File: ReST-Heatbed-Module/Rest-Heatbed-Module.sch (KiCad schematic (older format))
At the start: 16 parts, among them P1 02-SCREW-TERM, P2 02X04-MALE, P3 02-SCREW-TERM, P4 01X02-MALE, P5 02-SCREW-TERM, Q1 Q_BSH105, Q2 Q_AOT240L

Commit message: Moved Folders + Heatbed PCB Finished
If there is any problem, please post an issue or write a post on the stm32duino forum. I can assure there is going to be a problem again with the libraries used, would really appreciate it to get some suggestions onto how to manage that
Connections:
- net +3V3: now also P2.3 (P3); no longer P2.2 (P2)
- net +5V: now also P2.5 (P5), P2.6 (P6); no longer P2.1 (P1), P2.3 (P3)
- net GND: now also P1.2 (P2); no longer P1.1 (P1)
- net PWM-HEATBED: now also P2.1 (P1); no longer P2.6 (P6)
- net T0: now also P2.2 (P2); no longer P2.5 (P5)
- net at F1.1: now also P1.1 (P1); no longer P1.2 (P2)
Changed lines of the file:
@@
-$EndComp
-$Comp
-L CONN_02X04 P2
-U 1 1 56A6927C
-P 4750 2650
-F 0 "P2" H 4750 2900 50  0000 C CNN
-F 1 "02X04-MALE" H 4750 2400 50  0000 C CNN
-F 2 "Pin_Headers:Pin_Header_Angled_2x04" H 4750 1450 50  0001 C CNN
-F 3 "" H 4750 1450 50  0000 C CNN
-	1    4750 2650
-	1    0    0    -1
 $EndComp
 $Comp
@@
 F 3 "" H 2950 2550 50  0000 C CNN
 	1    2950 2550
-	-1   0    0    1
+	-1   0    0    -1
 $EndComp
 $Comp
@@
 L +5V #PWR05
 U 1 1 56A6A1BB
-P 4400 2400
-F 0 "#PWR05" H 4400 2250 50  0001 C CNN
-F 1 "+5V" H 4400 2540 50  0000 C CNN
-F 2 "" H 4400 2400 50  0000 C CNN
-F 3 "" H 4400 2400 50  0000 C CNN
-	1    4400 2400
+P 4300 2700
+F 0 "#PWR05" H 4300 2550 50  0001 C CNN
+F 1 "+5V" H 4300 2840 50  0000 C CNN
+F 2 "" H 4300 2700 50  0000 C CNN
+F 3 "" H 4300 2700 50  0000 C CNN
+	1    4300 2700
 	1    0    0    -1
 $EndComp
@@
 L +3V3 #PWR06
 U 1 1 56A6A1DD
-P 5100 2400
-F 0 "#PWR06" H 5100 2250 50  0001 C CNN
-F 1 "+3V3" H 5100 2540 50  0000 C CNN
-F 2 "" H 5100 2400 50  0000 C CNN
-F 3 "" H 5100 2400 50  0000 C CNN
-	1    5100 2400
-	1    0    0    -1
+P 5350 2600
+F 0 "#PWR06" H 5350 2450 50  0001 C CNN
+F 1 "+3V3" H 5350 2740 50  0000 C CNN
+F 2 "" H 5350 2600 50  0000 C CNN
+F 3 "" H 5350 2600 50  0000 C CNN
+	1    5350 2600
+	-1   0    0    1
 $EndComp
 $Comp
@@
 	3350 2600 3350 2700
 Wire Wire Line
-	4400 2400 4400 2600
-Wire Wire Line
-	4400 2500 4500 2500
-Wire Wire Line
-	5100 2400 5100 2600
-Wire Wire Line
-	5100 2500 5000 2500
-Wire Wire Line
-	4500 2800 4400 2800
-Wire Wire Line
-	4400 2800 4400 3000
-Wire Wire Line
-	4400 3000 5100 3000
-Wire Wire Line
-	5100 3000 5100 2800
-Wire Wire Line
-	5100 2800 5000 2800
-Wire Wire Line
-	4750 3000 4750 3100
-Connection ~ 4750 3000
-Wire Wire Line
-	4300 2700 4500 2700
-Wire Wire Line
-	5200 2700 5000 2700
-Wire Wire Line
-	4400 2600 4500 2600
-Connection ~ 4400 2500
-Wire Wire Line
-	5100 2600 5000 2600
-Connection ~ 5100 2500
-Wire Wire Line
 	6350 3000 6350 2550
 Wire Wire Line
@@
 	9950 2750 9750 2750
 Wire Wire Line
-	9750 2650 9750 2750
-Wire Wire Line
-	9550 2650 9750 2650
+	9750 2750 9750 2650
+Wire Wire Line
+	9750 2650 9550 2650
 Wire Wire Line
 	9950 2850 9750 2850
 Wire Wire Line
-	9750 2950 9750 2850
-Wire Wire Line
-	9550 2950 9750 2950
+	9750 2850 9750 2950
+Wire Wire Line
+	9750 2950 9550 2950
 Wire Wire Line
 	9650 2450 9650 2650
@@
 Text Label 7850 3850 2    39   ~ 0
 PWM-HEATBED
-Text Label 5200 2700 0    39   ~ 0
+Text Label 5200 2500 0    39   ~ 0
 PWM-HEATBED
-Text Label 4300 2700 2    39   ~ 0
+Text Label 4300 2500 2    39   ~ 0
 T0
 $Comp
@@
 Text Notes 2650 3550 0    39   ~ 0
 Power Definitions
+$Comp
+L CONN_02X04 P2
+U 1 1 56A6927C
+P 4750 2650
+F 0 "P2" H 4750 2900 50  0000 C CNN
+F 1 "02X04-MALE" H 4750 2400 50  0000 C CNN
+F 2 "Pin_Headers:Pin_Header_Angled_2x04" H 4750 1450 50  0001 C CNN
+F 3 "" H 4750 1450 50  0000 C CNN
+	1    4750 2650
+	-1   0    0    -1
+$EndComp
+Wire Wire Line
+	4750 3100 4750 3050
+Wire Wire Line
+	4400 3050 5100 3050
+Wire Wire Line
+	4400 3050 4400 2800
+Wire Wire Line
+	4400 2800 4500 2800
+Wire Wire Line
+	5100 3050 5100 2800
+Wire Wire Line
+	5100 2800 5000 2800
+Connection ~ 4750 3050
+Wire Wire Line
+	5000 2500 5200 2500
+Wire Wire Line
+	4500 2500 4300 2500
+Wire Wire Line
+	4300 2700 5000 2700
+Wire Wire Line
+	4500 2600 5350 2600
+Connection ~ 5000 2600
+Connection ~ 4500 2700
 $EndSCHEMATC

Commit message: PRE-RELEASE Rev. A!
Yay. I managed to finish the Main PCB over the night, must say, Im happy with it. Things that changed since the last release:

Heater:
-Heater Module uses less Pins
- Much smaller Design now

Heatbed & Additional Module: 
-Changed distance from Edge to first Pin from 2.5mm to 2mm (will be changed on other boards too)

Mainboard:
-Added I2C Pullups 4K7
-Swapped Pins from Stepper, Heaters and Endstops around for easier PCB Design.
-Finished Design (10cm x 10cm!)

Added some 3D Models for testing. If someone has problems with loading some modules, please contact me! (or make a pull request with a better solution)
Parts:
- C1: footprint ok-smd-generic:1206 -> Capacitors_SMD:C_1206_HandSoldering
- R1, R2, R3, R4, R5: footprint ok-smd-generic:1206 -> Resistors_SMD:R_1206_HandSoldering
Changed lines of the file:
@@
 F 0 "R4" V 8680 3550 50  0000 C CNN
 F 1 "22R" V 8600 3550 50  0000 C CNN
-F 2 "ok-smd-generic:1206" V 8530 3550 50  0001 C CNN
+F 2 "Resistors_SMD:R_1206_HandSoldering" V 8530 3550 50  0001 C CNN
 F 3 "" H 8600 3550 50  0000 C CNN
 	1    8600 3550
@@
 F 0 "C1" H 6425 4050 50  0000 L CNN
 F 1 "10uF" H 6425 3850 50  0000 L CNN
-F 2 "ok-smd-generic:1206" H 6438 3800 50  0001 C CNN
+F 2 "Capacitors_SMD:C_1206_HandSoldering" H 6438 3800 50  0001 C CNN
 F 3 "" H 6400 3950 50  0000 C CNN
 	1    6400 3950
@@
 F 0 "R1" V 6480 3550 50  0000 C CNN
 F 1 "4.7K" V 6400 3550 50  0000 C CNN
-F 2 "ok-smd-generic:1206" V 6330 3550 50  0001 C CNN
+F 2 "Resistors_SMD:R_1206_HandSoldering" V 6330 3550 50  0001 C CNN
 F 3 "" H 6400 3550 50  0000 C CNN
 	1    6400 3550
@@
 F 0 "R2" V 8030 3600 50  0000 C CNN
 F 1 "100K" V 7950 3600 50  0000 C CNN
-F 2 "ok-smd-generic:1206" V 7880 3600 50  0001 C CNN
+F 2 "Resistors_SMD:R_1206_HandSoldering" V 7880 3600 50  0001 C CNN
 F 3 "" H 7950 3600 50  0000 C CNN
 	1    7950 3600
@@
 F 0 "R3" V 8430 3300 50  0000 C CNN
 F 1 "100K" V 8350 3300 50  0000 C CNN
-F 2 "ok-smd-generic:1206" V 8280 3300 50  0001 C CNN
+F 2 "Resistors_SMD:R_1206_HandSoldering" V 8280 3300 50  0001 C CNN
 F 3 "" H 8350 3300 50  0000 C CNN
 	1    8350 3300
@@
 F 0 "R5" V 8830 2950 50  0000 C CNN
 F 1 "470R" V 8750 2950 50  0000 C CNN
-F 2 "ok-smd-generic:1206" V 8680 2950 50  0001 C CNN
+F 2 "Resistors_SMD:R_1206_HandSoldering" V 8680 2950 50  0001 C CNN
 F 3 "" H 8750 2950 50  0000 C CNN
 	1    8750 2950

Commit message: Finally removed all unnecessary Libs and added Heatsink for 5V Regulator
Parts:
- Q1: footprint TO_SOT_Packages_SMD:SOT-23 -> ReST-Library:SOT-23
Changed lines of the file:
@@
 LIBS:dc-dc
 LIBS:diode
-LIBS:dp_devices
 LIBS:elec-unifil
 LIBS:ESD_Protection
@@
 LIBS:nordicsemi
 LIBS:nxp_armmcu
-LIBS:ok-74logic
-LIBS:ok-con-generic
-LIBS:ok-diodes
-LIBS:ok-generic
-LIBS:ok-ic-analog
-LIBS:ok-ic-atmel
-LIBS:ok-ic-com
-LIBS:ok-ic-memory
-LIBS:ok-ic-power
-LIBS:ok-ic-special
-LIBS:ok-ic-stm32
-LIBS:ok-jacks
-LIBS:ok-opto
-LIBS:ok-power
-LIBS:ok-relay
-LIBS:ok-switches
-LIBS:ok-transformers
-LIBS:ok-transistors
 LIBS:onsemi
 LIBS:Oscillators
-LIBS:pololu_a4988
 LIBS:Power_Management
 LIBS:powerint
@@
 F 0 "Q1" H 8550 3900 50  0000 R CNN
 F 1 "Q_BSH105" H 8900 3800 50  0000 R CNN
-F 2 "TO_SOT_Packages_SMD:SOT-23" H 8450 3950 50  0001 C CNN
+F 2 "ReST-Library:SOT-23" H 8450 3950 50  0001 C CNN
 F 3 "" H 8250 3850 50  0000 C CNN
 	1    8250 3850

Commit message: Added BOM for all Items + suggested Links
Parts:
- R5: value 470R -> 150R
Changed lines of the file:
@@
 P 8750 2950
 F 0 "R5" V 8830 2950 50  0000 C CNN
-F 1 "470R" V 8750 2950 50  0000 C CNN
+F 1 "150R" V 8750 2950 50  0000 C CNN
 F 2 "Resistors_SMD:R_1206_HandSoldering" V 8680 2950 50  0001 C CNN
 F 3 "" H 8750 2950 50  0000 C CNN

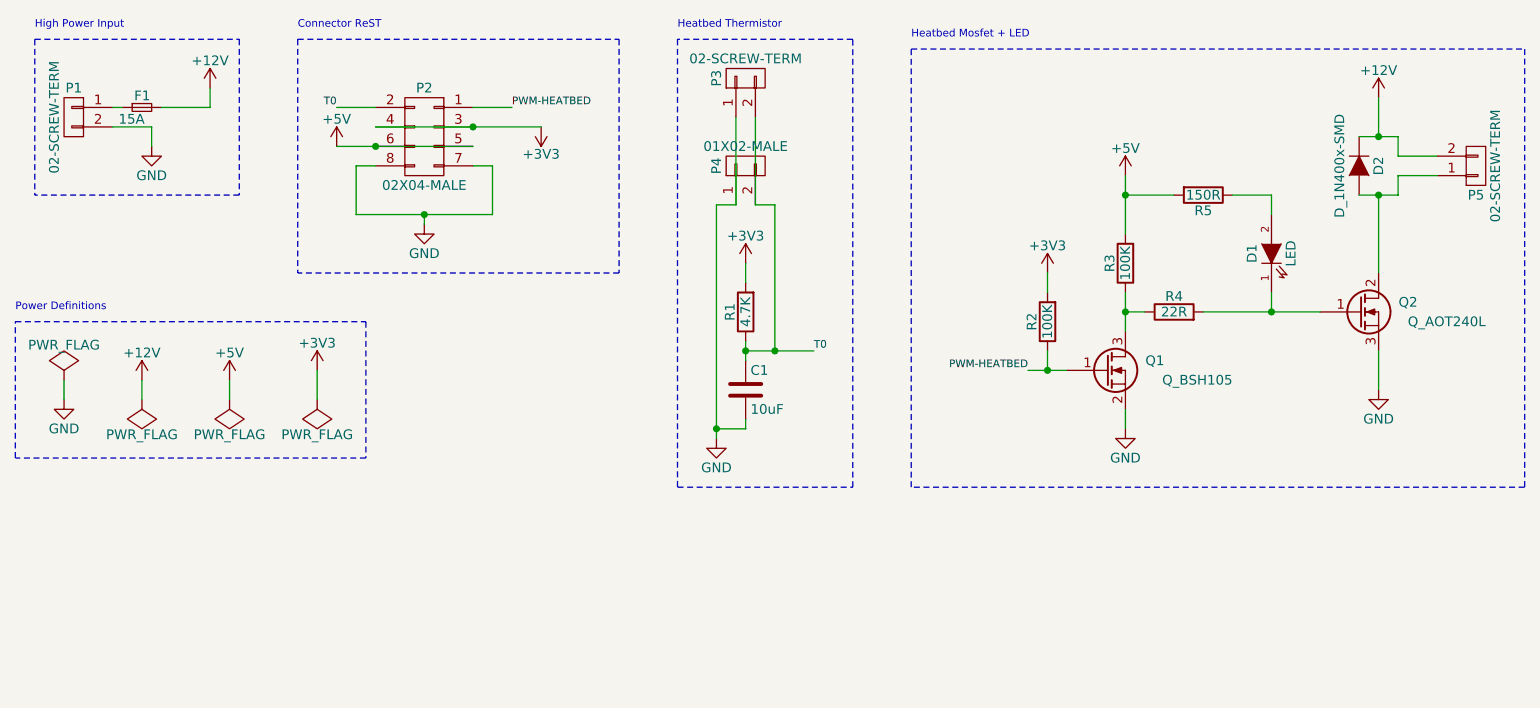
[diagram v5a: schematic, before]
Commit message: Reworked Modules to sit ontop of the mainboard
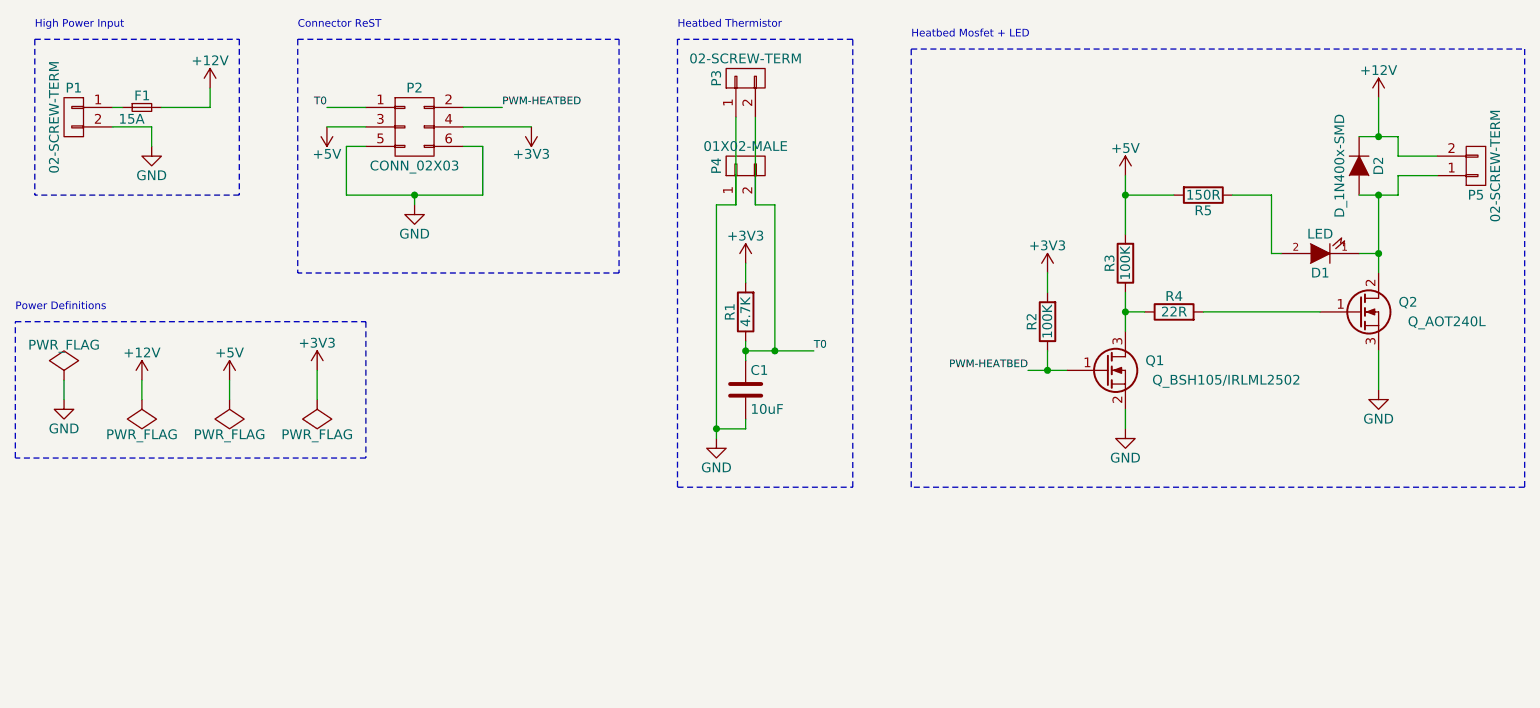
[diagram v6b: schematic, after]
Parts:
- removed P2: 02X04-MALE, Pin_Headers:Pin_Header_Angled_2x04, symbol CONN_02X04
- added P2: CONN_02X03, ReST-Library:bb02-hp06, symbol CONN_02X03
- C1: footprint Capacitors_SMD:C_1206_HandSoldering -> Capacitors_SMD:C_0805_HandSoldering
- D1: footprint LEDs:LED_1206 -> LEDs:LED_0805
- D2: footprint DO-214AC(SMA):DO-214AC(SMA) -> ReST-Library:DO-214AC.SMA
- F1: footprint ReST-Librar:JEF-703C -> ReST-Library:MINI-FUSE
- P1, P5: footprint 5mm-pitch-terminal:mkds_1,5-2 -> ReST-Library:screw-5-2P
- P3: footprint 2:mpt_0,5%2f2-2,54 -> ReST-Library:pt_1,5-2-3,5-h
- Q1: value Q_BSH105 -> Q_BSH105/IRLML2502
- Q2: footprint TO_SOT_Packages_THT:TO-220_Neutral123_Vertical_LargePads -> ReST-Library:TO-220_Neutral123_Vertical_LargePads_Heatsink
- R1, R2, R3, R4, R5: footprint Resistors_SMD:R_1206_HandSoldering -> Resistors_SMD:R_0805_HandSoldering
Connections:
- net +3V3: now also P2.4 (P4)
- net +5V: now also P2.3 (P3)
- net GND: now also P2.5 (P5), P2.6 (P6)
- net PWM-HEATBED: now also P2.2 (P2)
- net T0: now also P2.1 (P1)
- net at Q2.1 (G), R4.2: no longer D1.1 (K)
- net at D2.2 (A), P5.1 (P1), Q2.2 (D): now also D1.1 (K)
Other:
- moved on the sheet: D1
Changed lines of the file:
@@
 F 0 "Q2" H 9850 3600 50  0000 R CNN
 F 1 "Q_AOT240L" H 10200 3500 50  0000 R CNN
-F 2 "TO_SOT_Packages_THT:TO-220_Neutral123_Vertical_LargePads" H 9750 3650 50  0001 C CNN
+F 2 "ReST-Library:TO-220_Neutral123_Vertical_LargePads_Heatsink" H 9750 3650 50  0001 C CNN
 F 3 "" H 9550 3550 50  0000 C CNN
 	1    9550 3550
@@
 F 0 "P5" H 10150 2950 50  0000 C CNN
 F 1 "02-SCREW-TERM" V 10250 2800 50  0000 C CNN
-F 2 "5mm-pitch-terminal:mkds_1,5-2" H 10150 2800 50  0001 C CNN
+F 2 "ReST-Library:screw-5-2P" H 10150 2800 50  0001 C CNN
 F 3 "" H 10150 2800 50  0000 C CNN
 	1    10150 2800
@@
 P 8250 3850
 F 0 "Q1" H 8550 3900 50  0000 R CNN
-F 1 "Q_BSH105" H 8900 3800 50  0000 R CNN
+F 1 "Q_BSH105/IRLML2502" H 9250 3800 50  0000 R CNN
 F 2 "ReST-Library:SOT-23" H 8450 3950 50  0001 C CNN
 F 3 "" H 8250 3850 50  0000 C CNN
@@
 F 0 "D2" H 9550 2900 50  0000 C CNN
 F 1 "D_1N400x-SMD" H 9550 2700 50  0000 C CNN
-F 2 "DO-214AC(SMA):DO-214AC(SMA)" H 9550 2800 50  0001 C CNN
+F 2 "ReST-Library:DO-214AC.SMA" H 9550 2800 50  0001 C CNN
 F 3 "" H 9550 2800 50  0000 C CNN
 	1    9550 2800
@@
 F 0 "R4" V 8680 3550 50  0000 C CNN
 F 1 "22R" V 8600 3550 50  0000 C CNN
-F 2 "Resistors_SMD:R_1206_HandSoldering" V 8530 3550 50  0001 C CNN
+F 2 "Resistors_SMD:R_0805_HandSoldering" V 8530 3550 50  0001 C CNN
 F 3 "" H 8600 3550 50  0000 C CNN
 	1    8600 3550
@@
 F 0 "P1" H 2950 2700 50  0000 C CNN
 F 1 "02-SCREW-TERM" V 3050 2550 50  0000 C CNN
-F 2 "5mm-pitch-terminal:mkds_1,5-2" H 2950 2550 50  0001 C CNN
+F 2 "ReST-Library:screw-5-2P" H 2950 2550 50  0001 C CNN
 F 3 "" H 2950 2550 50  0000 C CNN
 	1    2950 2550
@@
 L +5V #PWR05
 U 1 1 56A6A1BB
-P 4300 2700
-F 0 "#PWR05" H 4300 2550 50  0001 C CNN
-F 1 "+5V" H 4300 2840 50  0000 C CNN
-F 2 "" H 4300 2700 50  0000 C CNN
-F 3 "" H 4300 2700 50  0000 C CNN
-	1    4300 2700
-	1    0    0    -1
+P 4250 2600
+F 0 "#PWR05" H 4250 2450 50  0001 C CNN
+F 1 "+5V" H 4250 2740 50  0000 C CNN
+F 2 "" H 4250 2600 50  0000 C CNN
+F 3 "" H 4250 2600 50  0000 C CNN
+	1    4250 2600
+	-1   0    0    1
 $EndComp
 $Comp
 L +3V3 #PWR06
 U 1 1 56A6A1DD
-P 5350 2600
-F 0 "#PWR06" H 5350 2450 50  0001 C CNN
-F 1 "+3V3" H 5350 2740 50  0000 C CNN
-F 2 "" H 5350 2600 50  0000 C CNN
-F 3 "" H 5350 2600 50  0000 C CNN
-	1    5350 2600
+P 5300 2600
+F 0 "#PWR06" H 5300 2450 50  0001 C CNN
+F 1 "+3V3" H 5300 2740 50  0000 C CNN
+F 2 "" H 5300 2600 50  0000 C CNN
+F 3 "" H 5300 2600 50  0000 C CNN
+	1    5300 2600
 	-1   0    0    1
 $EndComp
@@
 L GND #PWR07
 U 1 1 56A6A1FF
-P 4750 3100
-F 0 "#PWR07" H 4750 2850 50  0001 C CNN
-F 1 "GND" H 4750 2950 50  0000 C CNN
-F 2 "" H 4750 3100 50  0000 C CNN
-F 3 "" H 4750 3100 50  0000 C CNN
-	1    4750 3100
+P 4700 3000
+F 0 "#PWR07" H 4700 2750 50  0001 C CNN
+F 1 "GND" H 4700 2850 50  0000 C CNN
+F 2 "" H 4700 3000 50  0000 C CNN
+F 3 "" H 4700 3000 50  0000 C CNN
+	1    4700 3000
 	1    0    0    -1
 $EndComp
@@
 F 0 "P3" H 6400 2500 50  0000 C CNN
 F 1 "02-SCREW-TERM" V 6500 2350 50  0000 C CNN
-F 2 "2:mpt_0,5%2f2-2,54" H 6400 2350 50  0001 C CNN
+F 2 "ReST-Library:pt_1,5-2-3,5-h" H 6400 2350 50  0001 C CNN
 F 3 "" H 6400 2350 50  0000 C CNN
 	1    6400 2350
@@
 F 0 "C1" H 6425 4050 50  0000 L CNN
 F 1 "10uF" H 6425 3850 50  0000 L CNN
-F 2 "Capacitors_SMD:C_1206_HandSoldering" H 6438 3800 50  0001 C CNN
+F 2 "Capacitors_SMD:C_0805_HandSoldering" H 6438 3800 50  0001 C CNN
 F 3 "" H 6400 3950 50  0000 C CNN
 	1    6400 3950
@@
 F 0 "R1" V 6480 3550 50  0000 C CNN
 F 1 "4.7K" V 6400 3550 50  0000 C CNN
-F 2 "Resistors_SMD:R_1206_HandSoldering" V 6330 3550 50  0001 C CNN
+F 2 "Resistors_SMD:R_0805_HandSoldering" V 6330 3550 50  0001 C CNN
 F 3 "" H 6400 3550 50  0000 C CNN
 	1    6400 3550
@@
 F 0 "R2" V 8030 3600 50  0000 C CNN
 F 1 "100K" V 7950 3600 50  0000 C CNN
-F 2 "Resistors_SMD:R_1206_HandSoldering" V 7880 3600 50  0001 C CNN
+F 2 "Resistors_SMD:R_0805_HandSoldering" V 7880 3600 50  0001 C CNN
 F 3 "" H 7950 3600 50  0000 C CNN
 	1    7950 3600
@@
 F 0 "R3" V 8430 3300 50  0000 C CNN
 F 1 "100K" V 8350 3300 50  0000 C CNN
-F 2 "Resistors_SMD:R_1206_HandSoldering" V 8280 3300 50  0001 C CNN
+F 2 "Resistors_SMD:R_0805_HandSoldering" V 8280 3300 50  0001 C CNN
 F 3 "" H 8350 3300 50  0000 C CNN
 	1    8350 3300
@@
 F 0 "F1" H 3260 2560 50  0000 L CNN
 F 1 "15A" H 3180 2440 50  0000 L CNN
-F 2 "ReST-Librar:JEF-703C" H 3300 2500 50  0001 C CNN
+F 2 "ReST-Library:MINI-FUSE" H 3300 2500 50  0001 C CNN
 F 3 "" H 3300 2500 50  0000 C CNN
 	1    3300 2500
@@
 F 0 "R5" V 8830 2950 50  0000 C CNN
 F 1 "150R" V 8750 2950 50  0000 C CNN
-F 2 "Resistors_SMD:R_1206_HandSoldering" V 8680 2950 50  0001 C CNN
+F 2 "Resistors_SMD:R_0805_HandSoldering" V 8680 2950 50  0001 C CNN
 F 3 "" H 8750 2950 50  0000 C CNN
 	1    8750 2950
@@
 L LED D1
 U 1 1 56A70EAE
-P 9100 3250
-F 0 "D1" H 9100 3350 50  0000 C CNN
-F 1 "LED" H 9100 3150 50  0000 C CNN
-F 2 "LEDs:LED_1206" H 9100 3250 50  0001 C CNN
-F 3 "" H 9100 3250 50  0000 C CNN
-	1    9100 3250
-	0    -1   -1   0
+P 9350 3250
+F 0 "D1" H 9350 3350 50  0000 C CNN
+F 1 "LED" H 9350 3150 50  0000 C CNN
+F 2 "LEDs:LED_0805" H 9350 3250 50  0001 C CNN
+F 3 "" H 9350 3250 50  0000 C CNN
+	1    9350 3250
+	-1   0    0    1
 $EndComp
 Text Notes 7250 2150 0    39   ~ 0
@@
 Wire Wire Line
 	9650 3950 9650 3750
-Connection ~ 9100 3550
 Wire Wire Line
 	3150 2500 3200 2500
@@
 Connection ~ 9650 2950
 Wire Wire Line
-	9100 3550 9100 3450
-Wire Wire Line
-	9100 3050 9100 2950
+	9100 2950 9100 3250
 Wire Wire Line
 	9100 2950 8900 2950
@@
 Text Label 7850 3850 2    39   ~ 0
 PWM-HEATBED
-Text Label 5200 2500 0    39   ~ 0
+Text Label 5150 2500 0    39   ~ 0
 PWM-HEATBED
-Text Label 4300 2500 2    39   ~ 0
+Text Label 4250 2500 2    39   ~ 0
 T0
 $Comp
@@
 Text Notes 2650 3550 0    39   ~ 0
 Power Definitions
-$Comp
-L CONN_02X04 P2
-U 1 1 56A6927C
-P 4750 2650
-F 0 "P2" H 4750 2900 50  0000 C CNN
-F 1 "02X04-MALE" H 4750 2400 50  0000 C CNN
-F 2 "Pin_Headers:Pin_Header_Angled_2x04" H 4750 1450 50  0001 C CNN
-F 3 "" H 4750 1450 50  0000 C CNN
-	1    4750 2650
-	-1   0    0    -1
-$EndComp
-Wire Wire Line
-	4750 3100 4750 3050
-Wire Wire Line
-	4400 3050 5100 3050
-Wire Wire Line
-	4400 3050 4400 2800
-Wire Wire Line
-	4400 2800 4500 2800
-Wire Wire Line
-	5100 3050 5100 2800
-Wire Wire Line
-	5100 2800 5000 2800
-Connection ~ 4750 3050
-Wire Wire Line
-	5000 2500 5200 2500
-Wire Wire Line
-	4500 2500 4300 2500
-Wire Wire Line
-	4300 2700 5000 2700
-Wire Wire Line
-	4500 2600 5350 2600
-Connection ~ 5000 2600
-Connection ~ 4500 2700
+Wire Wire Line
+	4700 3000 4700 2950
+Wire Wire Line
+	4350 2950 5050 2950
+Wire Wire Line
+	4350 2950 4350 2700
+Wire Wire Line
+	4350 2700 4450 2700
+Wire Wire Line
+	5050 2950 5050 2700
+Wire Wire Line
+	5050 2700 4950 2700
+Connection ~ 4700 2950
+Wire Wire Line
+	4950 2500 5150 2500
+Wire Wire Line
+	4450 2500 4250 2500
+Wire Wire Line
+	9100 3250 9150 3250
+Wire Wire Line
+	9550 3250 9650 3250
+Connection ~ 9650 3250
+$Comp
+L CONN_02X03 P2
+U 1 1 572F92E1
+P 4700 2600
+F 0 "P2" H 4700 2800 50  0000 C CNN
+F 1 "CONN_02X03" H 4700 2400 50  0000 C CNN
+F 2 "ReST-Library:bb02-hp06" H 4700 1400 50  0001 C CNN
+F 3 "" H 4700 1400 50  0000 C CNN
+	1    4700 2600
+	1    0    0    -1
+$EndComp
+Wire Wire Line
+	4250 2600 4450 2600
+Wire Wire Line
+	5300 2600 4950 2600
 $EndSCHEMATC
